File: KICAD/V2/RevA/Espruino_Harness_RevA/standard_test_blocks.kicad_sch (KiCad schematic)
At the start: 0 parts

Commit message: Implement Target Interface and GPIO loopback
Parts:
- added JP101: LOOP_A_ISOLATION, Connector_PinHeader_2.54mm:PinHeader_1x02_P2.54mm_Vertical, symbol Jumper:Jumper_2_Open
- added JP102: LOOP_B_ISOLATION, Connector_PinHeader_2.54mm:PinHeader_1x02_P2.54mm_Vertical, symbol Jumper:Jumper_2_Open
- added R101, R102: 470R, symbol Device:R
- added TP101: LOOP_A_OUT, Connector_PinHeader_2.54mm:PinHeader_1x01_P2.54mm_Vertical, symbol Connector:TestPoint
- added TP102: LOOP_A_IN, Connector_PinHeader_2.54mm:PinHeader_1x01_P2.54mm_Vertical, symbol Connector:TestPoint
- added TP103: LOOP_B_OUT, Connector_PinHeader_2.54mm:PinHeader_1x01_P2.54mm_Vertical, symbol Connector:TestPoint
- added TP104: LOOP_B_IN, Connector_PinHeader_2.54mm:PinHeader_1x01_P2.54mm_Vertical, symbol Connector:TestPoint
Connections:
- new net: JP101.1 (A), R101.2
- new net: JP102.1 (A), R102.2
- new net TI_GPIO_LOOP_A_IN: JP101.2 (B), TP102.1
- new net TI_GPIO_LOOP_A_OUT: R101.1, TP101.1
- new net TI_GPIO_LOOP_B_IN: JP102.2 (B), TP104.1
- new net TI_GPIO_LOOP_B_OUT: R102.1, TP103.1
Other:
- note added: "BLOCK 1 - DIGITAL GPIO LOOPBACK"
- note added: "PAIR A"
- note added: "PAIR B"

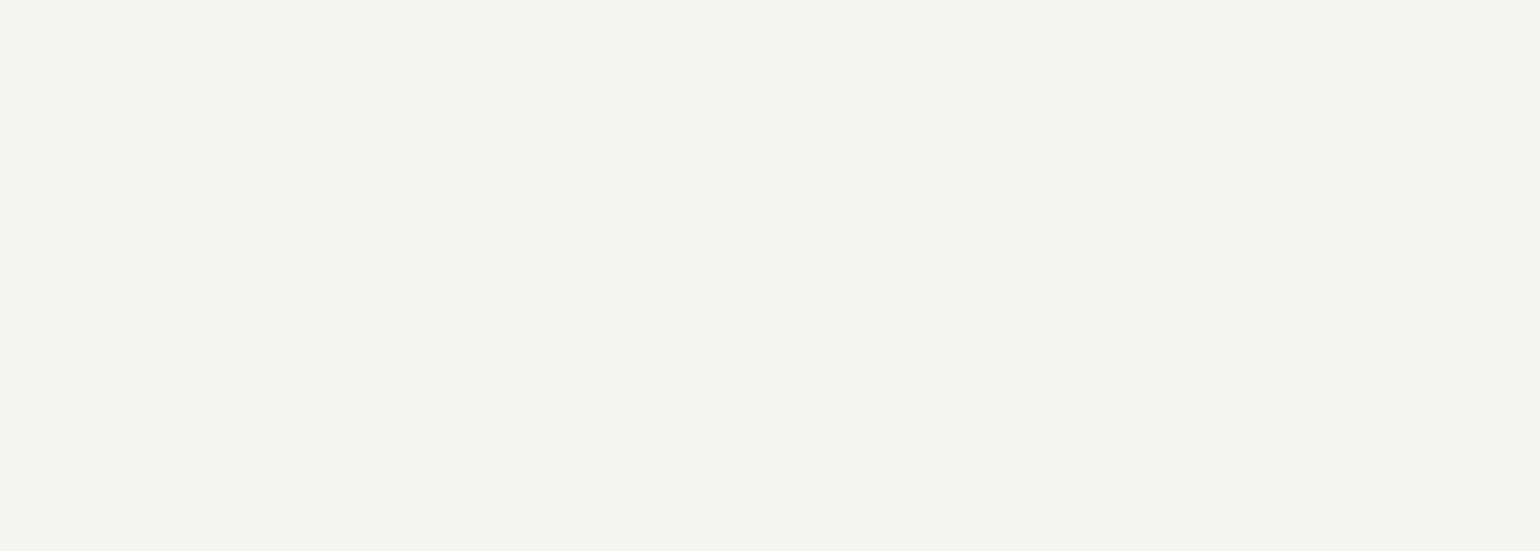
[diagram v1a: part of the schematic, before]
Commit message: Add analogue PWM feedback test block
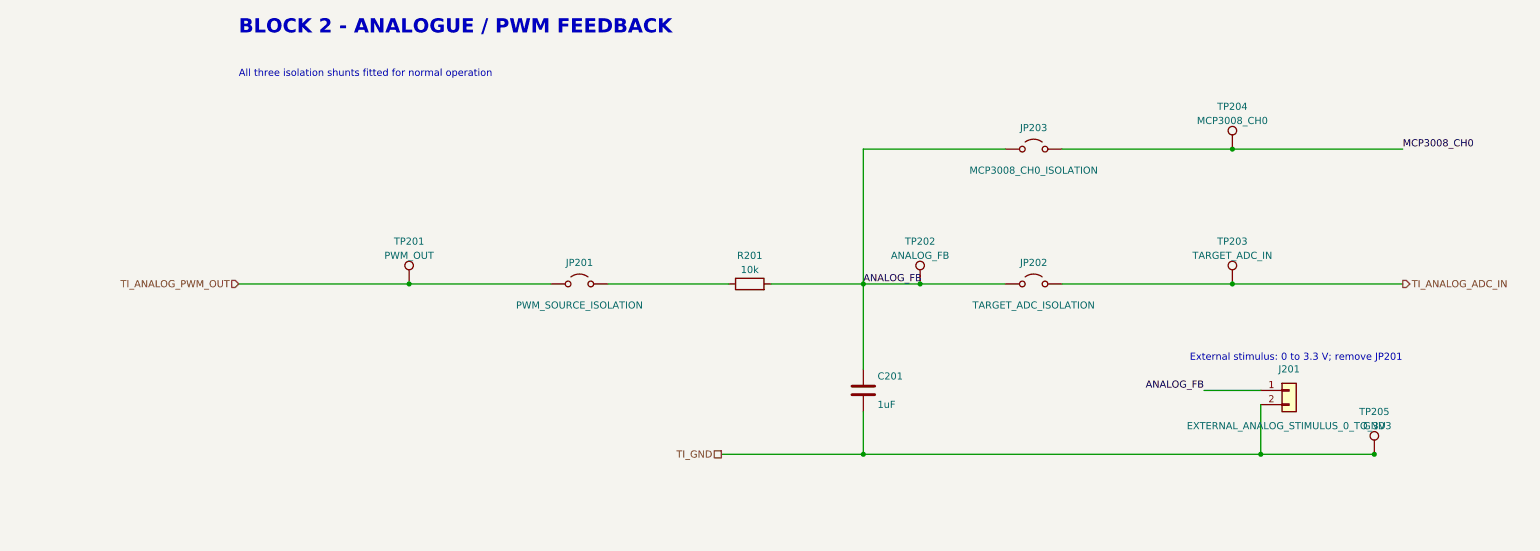
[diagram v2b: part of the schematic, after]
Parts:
- added C201: 1uF, symbol Device:C
- added J201: EXTERNAL_ANALOG_STIMULUS_0_TO_3V3, Connector_PinHeader_2.54mm:PinHeader_1x02_P2.54mm_Vertical, symbol Connector_Generic:Conn_01x02
- added JP201: PWM_SOURCE_ISOLATION, Connector_PinHeader_2.54mm:PinHeader_1x02_P2.54mm_Vertical, symbol Jumper:Jumper_2_Open
- added JP202: TARGET_ADC_ISOLATION, Connector_PinHeader_2.54mm:PinHeader_1x02_P2.54mm_Vertical, symbol Jumper:Jumper_2_Open
- added JP203: MCP3008_CH0_ISOLATION, Connector_PinHeader_2.54mm:PinHeader_1x02_P2.54mm_Vertical, symbol Jumper:Jumper_2_Open
- added R201: 10k, symbol Device:R
- added TP201: PWM_OUT, Connector_PinHeader_2.54mm:PinHeader_1x01_P2.54mm_Vertical, symbol Connector:TestPoint
- added TP202: ANALOG_FB, Connector_PinHeader_2.54mm:PinHeader_1x01_P2.54mm_Vertical, symbol Connector:TestPoint
- added TP203: TARGET_ADC_IN, Connector_PinHeader_2.54mm:PinHeader_1x01_P2.54mm_Vertical, symbol Connector:TestPoint
- added TP204: MCP3008_CH0, Connector_PinHeader_2.54mm:PinHeader_1x01_P2.54mm_Vertical, symbol Connector:TestPoint
- added TP205: GND, Connector_PinHeader_2.54mm:PinHeader_1x01_P2.54mm_Vertical, symbol Connector:TestPoint
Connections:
- new net: JP201.2 (B), R201.1
- new net ANALOG_FB: C201.1, J201.1 (Pin_1), JP202.1 (A), JP203.1 (A), R201.2, TP202.1
- new net MCP3008_CH0: JP203.2 (B), TP204.1
- new net TI_ANALOG_ADC_IN: JP202.2 (B), TP203.1
- new net TI_ANALOG_PWM_OUT: JP201.1 (A), TP201.1
- new net TI_GND: C201.2, J201.2 (Pin_2), TP205.1
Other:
- note added: "All three isolation shunts fitted for normal operation"
- note added: "BLOCK 2 - ANALOGUE / PWM FEEDBACK"
- note added: "External stimulus: 0 to 3.3 V; remove JP201"

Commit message: Implement V2 I2C functional test block
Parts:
- added C301: 100nF, symbol Device:C
- added J301: GROVE_I2C, symbol Espruino_Harness_RevA:Grove_I2C_1x04
- added J302: MCP23017_GPIO, Connector_PinHeader_2.54mm:PinHeader_2x08_P2.54mm_Vertical, symbol Espruino_Harness_RevA:MCP23017_Breakout_2x08
- added JP301: VDD_ISOLATION, Connector_PinHeader_2.54mm:PinHeader_1x02_P2.54mm_Vertical, symbol Jumper:Jumper_2_Open
- added JP302: SDA_DEVICE_ISOLATION, Connector_PinHeader_2.54mm:PinHeader_1x02_P2.54mm_Vertical, symbol Jumper:Jumper_2_Open
- added JP303: SCL_DEVICE_ISOLATION, Connector_PinHeader_2.54mm:PinHeader_1x02_P2.54mm_Vertical, symbol Jumper:Jumper_2_Open
- added JP304: EVENT_INPUT_ISOLATION, Connector_PinHeader_2.54mm:PinHeader_1x02_P2.54mm_Vertical, symbol Jumper:Jumper_2_Open
- added JP306: FB_DEVICE_ISOLATION, Connector_PinHeader_2.54mm:PinHeader_1x02_P2.54mm_Vertical, symbol Jumper:Jumper_2_Open
- added JP307: INT_DEVICE_ISOLATION, Connector_PinHeader_2.54mm:PinHeader_1x02_P2.54mm_Vertical, symbol Jumper:Jumper_2_Open
- added JP308: SDA_PULLUP_ENABLE, Connector_PinHeader_2.54mm:PinHeader_1x02_P2.54mm_Vertical, symbol Jumper:Jumper_2_Open
- added JP309: SCL_PULLUP_ENABLE, Connector_PinHeader_2.54mm:PinHeader_1x02_P2.54mm_Vertical, symbol Jumper:Jumper_2_Open
- added Q301, Q302: 2N7002, Package_TO_SOT_SMD:SOT-23, symbol Espruino_Harness_RevA:NMOS_2N7002_GSD
- added R301, R302: 4.7k, Resistor_SMD:R_0603_1608Metric, symbol Device:R
- added R303, R304: 4.7k DNP, Resistor_SMD:R_0603_1608Metric, symbol Device:R
- added R305: 470R, symbol Device:R
- added R306: 10k, symbol Device:R
- added R307, R309, R310: 10k, Resistor_SMD:R_0603_1608Metric, symbol Device:R
- added R308, R311: 100k, Resistor_SMD:R_0603_1608Metric, symbol Device:R
- added TP301: SDA, Connector_PinHeader_2.54mm:PinHeader_1x01_P2.54mm_Vertical, symbol Connector:TestPoint
- added TP302: SCL, Connector_PinHeader_2.54mm:PinHeader_1x01_P2.54mm_Vertical, symbol Connector:TestPoint
- added TP303: TI_I2C_FB, Connector_PinHeader_2.54mm:PinHeader_1x01_P2.54mm_Vertical, symbol Connector:TestPoint
- added TP304: TI_I2C_INT, Connector_PinHeader_2.54mm:PinHeader_1x01_P2.54mm_Vertical, symbol Connector:TestPoint
- added TP305: 3V3, Connector_PinHeader_2.54mm:PinHeader_1x01_P2.54mm_Vertical, symbol Connector:TestPoint
- added TP306: GND, Connector_PinHeader_2.54mm:PinHeader_1x01_P2.54mm_Vertical, symbol Connector:TestPoint
- added U301: MCP23017-E/SO, Package_SO:SOIC-28W_7.5x17.9mm_P1.27mm, symbol Espruino_Harness_RevA:MCP23017_SO
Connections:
- net TI_GND: now also C301.2, J301.4 (GND), Q301.2 (S), Q302.2 (S), R308.2, R311.2, TP306.1, U301.10 (VSS)
- new net: Q301.1 (G), R307.2, R308.1
- new net: JP306.1 (A), R305.2
- new net: Q302.1 (G), R310.2, R311.1
- new net: JP304.1 (A), Q301.3 (D), R309.2
- new net: JP309.1 (A), R302.1, R304.1
- new net: JP308.1 (A), R301.1, R303.1
- new net: JP307.2 (B), U301.20 (INTA)
- new net I2C_SCL_BUS: J301.1 (SCL), JP303.2 (B), R302.2, R304.2, TP302.1, U301.12 (SCL)
- new net I2C_SDA_BUS: J301.2 (SDA), JP302.2 (B), R301.2, R303.2, TP301.1, U301.13 (SDA)
- new net IP03_TEST_BLOCK_SDA: JP302.1 (A)
- new net IP04_TEST_BLOCK_SCL: JP303.1 (A)
- new net MCP23017_RESET_N: R306.2, U301.18 (~{RESET})
- new net MCP23017_VDD: C301.1, JP301.1 (A), R309.1, U301.9 (VDD)
- new net MCP_GPA0: J302.1 (GPA0), R305.1, U301.21 (GPA0)
- new net MCP_GPA1: J302.3 (GPA1), J302.5 (GPA2), U301.22 (GPA1), U301.23 (GPA2)
- new net MCP_GPA3: J302.7 (GPA3), U301.24 (GPA3)
- new net MCP_GPA4: J302.9 (GPA4), U301.25 (GPA4)
- new net MCP_GPA5: J302.11 (GPA5), U301.26 (GPA5)
- new net MCP_GPA6: J302.13 (GPA6), U301.27 (GPA6)
- new net MCP_GPA7: J302.15 (GPA7), U301.28 (GPA7)
- new net MCP_GPB0: J302.2 (GPB0), JP304.2 (B), U301.1 (GPB0)
- new net MCP_GPB1: J302.4 (GPB1), R310.1, U301.2 (GPB1)
- new net MCP_GPB2: J302.6 (GPB2), U301.3 (GPB2)
- new net MCP_GPB3: J302.8 (GPB3), U301.4 (GPB3)
- new net MCP_GPB4: J302.10 (GPB4), U301.5 (GPB4)
- new net MCP_GPB5: J302.12 (GPB5), U301.6 (GPB5)
- new net MCP_GPB6: J302.14 (GPB6), U301.7 (GPB6)
- new net MCP_GPB7: J302.16 (GPB7), U301.8 (GPB7)
- new net SUP_EVENT_IN: Q302.3 (D)
- new net SUP_EVENT_OUT: R307.1
- new net TEST_BLOCK_3V3: J301.3 (3V3), JP301.2 (B), JP308.2 (B), JP309.2 (B), R306.1, TP305.1
- new net TI_I2C_FB: JP306.2 (B), TP303.1
- new net TI_I2C_INT: JP307.1 (A), TP304.1
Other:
- note added: "BLOCK 3 - I2C FUNCTIONAL DEVICE"
- note added: "BLOCK 3 OBSERVATION POINTS"
- note added: "CONFIGURABLE I2C PULL-UPS"
- note added: "GROVE I2C EXPANSION"
- note added: "INTA: mirrored, open-drain interrupt; INTB diagnostic"
- note added: "MCP23017 GPIO BREAKOUT"
- note added: "MCP23017 core - address 0x20"
- note added: "MCP_GPB1 high -> SUP_EVENT_IN low; Supervisor-side pull-up required"
- note added: "PROTECTED SUPERVISOR EVENT INTERFACE"
- note added: "R301/R302: 4.7k fitted; R303/R304: 4.7k DNP"
- note added: "SUP_EVENT_OUT high -> MCP_GPB0 low; JP304 isolates the MCP23017 input"

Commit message: Implement V2 SPI and 1-Wire test blocks
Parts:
- added C401, C402: 100nF, Capacitor_SMD:C_0603_1608Metric, symbol Device:C
- added C403: 22uF, Capacitor_SMD:C_0805_2012Metric, symbol Device:C
- added J401: MCP3008_ANALOGUE_BREAKOUT, Connector_PinHeader_2.54mm:PinHeader_1x08_P2.54mm_Vertical, symbol Espruino_Harness_RevA:MCP3008_Analogue_Breakout_1x08
- added J402: PIHUT_MICROSD_BREAKOUT_106696, Connector_PinHeader_2.54mm:PinHeader_1x09_P2.54mm_Vertical, symbol Espruino_Harness_RevA:PiHut_MicroSD_Breakout_1x09
- added J501: DS18B20_SENSOR_A, TerminalBlock_Phoenix:TerminalBlock_Phoenix_MPT-0,5-3-2.54_1x03_P2.54mm_Horizontal, symbol Connector_Generic:Conn_01x03
- added J502: DS18B20_SENSOR_B, TerminalBlock_Phoenix:TerminalBlock_Phoenix_MPT-0,5-3-2.54_1x03_P2.54mm_Horizontal, symbol Connector_Generic:Conn_01x03
- added J503: 2K2_DQ_4K7, Connector_PinHeader_2.54mm:PinHeader_1x03_P2.54mm_Vertical, symbol Jumper:Jumper_3_Open
- added J504: DS2413_MODULE, Connector_PinHeader_2.54mm:PinHeader_1x04_P2.54mm_Vertical, symbol Connector_Generic:Conn_01x04
- added R401, R402: 10k, Resistor_SMD:R_0603_1608Metric, symbol Device:R
- added R501: 2.2k, Resistor_SMD:R_0603_1608Metric, symbol Device:R
- added R502, R503, R504: 4.7k, Resistor_SMD:R_0603_1608Metric, symbol Device:R
- added R505, R506: 470R, Resistor_SMD:R_0603_1608Metric, symbol Device:R
- added TP401: TI_SPI_CS_ADC, Connector_PinHeader_2.54mm:PinHeader_1x01_P2.54mm_Vertical, symbol Connector:TestPoint
- added TP402, TP505: GND, Connector_PinHeader_2.54mm:PinHeader_1x01_P2.54mm_Vertical, symbol Connector:TestPoint
- added TP501: ONEWIRE_DQ, Connector_PinHeader_2.54mm:PinHeader_1x01_P2.54mm_Vertical, symbol Connector:TestPoint
- added TP502: ONEWIRE_PIOA, Connector_PinHeader_2.54mm:PinHeader_1x01_P2.54mm_Vertical, symbol Connector:TestPoint
- added TP503: ONEWIRE_PIOB, Connector_PinHeader_2.54mm:PinHeader_1x01_P2.54mm_Vertical, symbol Connector:TestPoint
- added TP504: 3V3, Connector_PinHeader_2.54mm:PinHeader_1x01_P2.54mm_Vertical, symbol Connector:TestPoint
- added U401: MCP3008, Package_DIP:DIP-16_W7.62mm_LongPads, symbol Espruino_Harness_RevA:MCP3008_DIP16
- C201, C301: footprint (none) -> Capacitor_SMD:C_0603_1608Metric
- R101, R102, R201, R305, R306: footprint (none) -> Resistor_SMD:R_0603_1608Metric
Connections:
- net ANALOG_FB: now also J401.1 (CH0), U401.1 (CH0)
- net TEST_BLOCK_3V3: now also C401.1, C402.1, C403.1, J402.4 (3V), J501.3 (Pin_3), J502.3 (Pin_3), R401.2, R402.1, R501.1, R502.1, R503.1, R504.1, TP504.1, U401.15 (VREF), U401.16 (VDD)
- net TI_GND: now also U301.15 (A0), U301.16 (A1), U301.17 (A2), C401.2, C402.2, C403.2, J402.5 (G), J501.1 (Pin_1), J502.1 (Pin_1), J504.4 (Pin_4), TP402.1, TP505.1, U401.14 (AGND), U401.9 (DGND)
- net MCP_GPA1 renamed MCP_GPA1_GPA2_LOOP
- new net: J401.2 (CH1), U401.2 (CH1)
- new net: J401.3 (CH2), U401.3 (CH2)
- new net: J401.4 (CH3), U401.4 (CH3)
- new net: J401.5 (CH4), U401.5 (CH4)
- new net: J401.6 (CH5), U401.6 (CH5)
- new net: J401.7 (CH6), U401.7 (CH6)
- new net: J401.8 (CH7), U401.8 (CH7)
- new net: J503.1 (A), R501.2
- new net: J503.3 (B), R502.2
- new net ONEWIRE_PIOA: J504.2 (Pin_2), R504.2, R505.1, TP502.1
- new net ONEWIRE_PIOB: J504.1 (Pin_1), R503.2, R506.1, TP503.1
- new net TI_ONEWIRE_DQ: J501.2 (Pin_2), J502.2 (Pin_2), J503.2 (C), J504.3 (Pin_3), TP501.1
- new net TI_ONEWIRE_GPIO_A_FB: R505.2
- new net TI_ONEWIRE_GPIO_B_FB: R506.2
- new net TI_SPI_CS_ADC: R401.1, TP401.1, U401.10 (CS/SHDN)
- new net TI_SPI_CS_EXT: J402.2 (CS), R402.2
- new net TI_SPI_MISO: J402.7 (DO), U401.12 (DOUT)
- new net TI_SPI_MOSI: J402.3 (DI), U401.11 (DIN)
- new net TI_SPI_SCK: J402.6 (CLK), U401.13 (CLK)
- no-connect marks 0 -> 4
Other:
- note added: "2K2 | DQ | 4K7; pins 2-3 normal"
- note added: "BLOCK 4 - SPI Functional Device And Removable Storage Extension"
- note added: "BLOCK 4A - SPI MCP3008 CORE"
- note added: "BLOCK 4B - MCP3008 ANALOGUE BREAKOUT"
- note added: "BLOCK 4C - REMOVABLE MICROSD EXTENSION"
- note added: "BLOCK 5 - 1-WIRE FUNCTIONAL DEVICES AND GPIO"
- note added: "BLOCK 5 OBSERVATION POINTS"
- note added: "DS18B20 SENSOR A"
- note added: "DS18B20 SENSOR B"
- note added: "INTA → TI_I2C_INT; INTA/INTB mirrored open-drain;"
- note added: "PROTECTED TARGET FEEDBACK"
- note added: "PULL-UP SELECTOR"
- note added: "Pi Hut SKU 106696; physical header order shown"
- note added: "Pin 1 = CH0 / ANALOG_FB observation only in normal operation"
- note added: "Pin 1 marker; module uses parasite power from DQ"
- note added: "Power LED and module pull-ups disabled"
- note added: "REMOVABLE DS2413 MODULE"
- note added: "Socketed DIP-16; CH0 = Block 2 ANALOG_FB"
- note added: "Two removable powered DS18B20 branches; removable DS2413 on the shared bus"
- note removed: "INTA: mirrored, open-drain interrupt; INTB diagnostic"
- moved on the sheet: C201, C301, J201, J301, J302, JP101, JP102, JP201, JP202, JP203, JP301, JP302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

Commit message: Complete V2 standard test block schematic
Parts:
- added C701, C901: 100nF, Capacitor_SMD:C_0603_1608Metric, symbol Device:C
- added J701: UART_PEER_DIAGNOSTIC, Connector_PinHeader_2.54mm:PinHeader_2x03_P2.54mm_Vertical, symbol Connector_Generic:Conn_02x03_Odd_Even
- added J902: PIXEL_SHIFTER_6066, Connector_PinHeader_2.54mm:PinHeader_1x04_P2.54mm_Horizontal, symbol Connector_Generic:Conn_01x04
- added R701, R702, R703, R704, R901: 470R, Resistor_SMD:R_0603_1608Metric, symbol Device:R
- added R705, R706, R707, R708: 100k, Resistor_SMD:R_0603_1608Metric, symbol Device:R
- added TP901: RGB_DATA_PROTECTED, Connector_PinHeader_2.54mm:PinHeader_1x01_P2.54mm_Vertical, symbol Connector:TestPoint
- added TP902: RGB_GND, Connector_PinHeader_2.54mm:PinHeader_1x01_P2.54mm_Vertical, symbol Connector:TestPoint
- added U701: TMUX1511, Package_SO:TSSOP-14_4.4x5mm_P0.65mm, symbol Espruino_Harness_RevA:TMUX1511_PW
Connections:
- net TEST_BLOCK_3V3: now also C901.1, J902.1 (Pin_1)
- net TI_GND: now also C701.2, C901.2, J701.5 (Pin_5), J701.6 (Pin_6), J902.2 (Pin_2), R705.2, R706.2, R707.2, R708.2, TP902.1, U701.7 (GND)
- new net: R704.1, U701.11 (D4)
- new net: R701.1, U701.3 (D1)
- new net: R702.1, U701.6 (D2)
- new net: R703.1, U701.8 (D3)
- new net RGB_DATA_PROTECTED: J902.3 (Pin_3), R901.2, TP901.1
- new net ROUTING_LOGIC_3V3: C701.1, U701.14 (VDD)
- new net TI_RGB_DATA: R901.1
- new net TI_UART_A_RX: R702.2, R704.2
- new net TI_UART_A_TX: U701.2 (S1), U701.9 (S3)
- new net TI_UART_B_RX: J701.4 (Pin_4), R701.2
- new net TI_UART_B_TX: J701.2 (Pin_2), U701.5 (S2)
- new net UART_PEER_RX: J701.1 (Pin_1), R703.2
- new net UART_PEER_TX: J701.3 (Pin_3), U701.12 (S4)
- new net UP01_EN: R705.1, U701.1 (SEL1)
- new net UP02_EN: R706.1, U701.4 (SEL2)
- new net UP03_EN: R707.1, U701.10 (SEL3)
- new net UP04_EN: R708.1, U701.13 (SEL4)
- no-connect marks 4 -> 5
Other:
- note added: "100k each; TMUX1511 internal pull-downs provide additional bias"
- note added: "2x3 EXTERNAL PEER / DIAGNOSTIC"
- note added: "BLOCK 7 - UART FUNCTIONAL CROSSLINK AND EXTERNAL PEER"
- note added: "BLOCK 9 - ADDRESSABLE RGB OUTPUT"
- note added: "EXTERNAL SAFE-STATE PULL-DOWNS"
- note added: "Even contacts: direct endpoint B TX/RX/GND"
- note added: "Header provides no power; external peer must use 3.3 V signalling and share TI_GND"
- note added: "Odd contacts: switched endpoint A TX/RX/GND"
- note added: "PIXEL SHIFTER INPUT"
- note added: "Pin 1 V; pin 2 GND; pin 3 DAT; pin 4 CLK / NC"
- note added: "Removable Adafruit Pixel Shifter 6066; protected 3.3 V data observation"
- note added: "Remove module for isolation; Module generates its own 5 V internally; the harness does not use or export it"
- note added: "TMUX1511 UART SWITCH"
- note added: "UP01/UP02: target crosslink; UP03/UP04: switched endpoint-A peer; modes are mutually exclusive"
- moved on the sheet: J501, J502, J503, J504, R501, R502, R503, R504, R505, R506, TP501, TP502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

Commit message: Implement V2 routing fabric and control
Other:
- moved on the sheet: U701
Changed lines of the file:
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@@
+	(wire
+		(pts
+			(xy 120.65 302.26) (xy 120.65 270.51)
+		)
+		(stroke
+			(width 0)
+			(type default)
+		)
+	)
 	(wire
 		(pts
@@
 	(wire
 		(pts
+			(xy 128.27 245.11) (xy 132.08 245.11)
+		)
+		(stroke
+			(width 0)
+			(type default)
+		)
+	)
+	(wire
+		(pts
 			(xy 514.35 114.3) (xy 514.35 113.03)
 		)
@@
 	(wire
 		(pts
+			(xy 128.27 256.54) (xy 132.08 256.54)
+		)
+		(stroke
+			(width 0)
+			(type default)
+		)
+	)
+	(wire
+		(pts
 			(xy 170.18 201.93) (xy 182.88 201.93)
 		)
@@
 	(wire
 		(pts
-			(xy 107.95 292.1) (xy 97.79 292.1)
+			(xy 110.49 292.1) (xy 97.79 292.1)
 		)
 		(stroke
@@
 	(wire
 		(pts
+			(xy 128.27 261.62) (xy 132.08 261.62)
+		)
+		(stroke
+			(width 0)
+			(type default)
+		)
+	)
+	(wire
+		(pts
 			(xy 38.1 196.85) (xy 86.36 196.85)
 		)
@@
 	(wire
 		(pts
+			(xy 128.27 250.19) (xy 132.08 250.19)
+		)
+		(stroke
+			(width 0)
+			(type default)
+		)
+	)
+	(wire
+		(pts
 			(xy 359.41 43.18) (xy 373.38 43.18)
 		)
@@
 	(wire
 		(pts
-			(xy 123.19 245.11) (xy 132.08 245.11)
-		)
-		(stroke
-			(width 0)
-			(type default)
-		)
-	)
-	(wire
-		(pts
 			(xy 139.7 245.11) (xy 149.86 245.11)
 		)
@@
 	(wire
 		(pts
-			(xy 123.19 250.19) (xy 132.08 250.19)
-		)
-		(stroke
-			(width 0)
-			(type default)
-		)
-	)
-	(wire
-		(pts
 			(xy 139.7 250.19) (xy 149.86 250.19)
 		)
@@
 	(wire
 		(pts
-			(xy 123.19 256.54) (xy 132.08 256.54)
-		)
-		(stroke
-			(width 0)
-			(type default)
-		)
-	)
-	(wire
-		(pts
 			(xy 139.7 256.54) (xy 149.86 256.54)
 		)
@@
 	(wire
 		(pts
-			(xy 123.19 261.62) (xy 132.08 261.62)
-		)
-		(stroke
-			(width 0)
-			(type default)
-		)
-	)
-	(wire
-		(pts
 			(xy 139.7 261.62) (xy 149.86 261.62)
 		)
@@
 	(wire
 		(pts
-			(xy 104.14 270.51) (xy 104.14 285.75)
-		)
-		(stroke
-			(width 0)
-			(type default)
-		)
-	)
-	(wire
-		(pts
-			(xy 72.39 285.75) (xy 104.14 285.75)
-		)
-		(stroke
-			(width 0)
-			(type default)
-		)
-	)
-	(wire
-		(pts
-			(xy 111.76 270.51) (xy 111.76 297.18)
-		)
-		(stroke
-			(width 0)
-			(type default)
-		)
-	)
-	(wire
-		(pts
-			(xy 72.39 297.18) (xy 111.76 297.18)
-		)
-		(stroke
-			(width 0)
-			(type default)
-		)
-	)
-	(wire
-		(pts
-			(xy 115.57 270.51) (xy 115.57 302.26)
-		)
-		(stroke
-			(width 0)
-			(type default)
-		)
-	)
-	(wire
-		(pts
-			(xy 72.39 302.26) (xy 115.57 302.26)
+			(xy 105.41 270.51) (xy 105.41 285.75)
+		)
+		(stroke
+			(width 0)
+			(type default)
+		)
+	)
+	(wire
+		(pts
+			(xy 72.39 285.75) (xy 105.41 285.75)
+		)
+		(stroke
+			(width 0)
+			(type default)
+		)
+	)
+	(wire
+		(pts
+			(xy 115.57 270.51) (xy 115.57 297.18)
+		)
+		(stroke
+			(width 0)
+			(type default)
+		)
+	)
+	(wire
+		(pts
+			(xy 72.39 297.18) (xy 115.57 297.18)
+		)
+		(stroke
+			(width 0)
+			(type default)
+		)
+	)
+	(wire
+		(pts
+			(xy 72.39 302.26) (xy 120.65 302.26)
 		)
 		(stroke
@@
 	(wire
 		(pts
-			(xy 107.95 292.1) (xy 107.95 270.51)
-		)
-		(stroke
+			(xy 110.49 292.1) (xy 110.49 270.51)
+		)
+		(stroke
